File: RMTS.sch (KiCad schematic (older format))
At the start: 59 parts, among them J1 USB_B_Mini, J10 CONN_02, J2 Programmer, J3 Screw_Terminal_01x03, J4 Screw_Terminal_01x04, J5 Screw_Terminal_01x02, J6 Screw_Terminal_01x02, J7 Micro_SD_Card_Det_Hirose_DM3AT, J9 CONN_02, Q1 PMV20ENR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

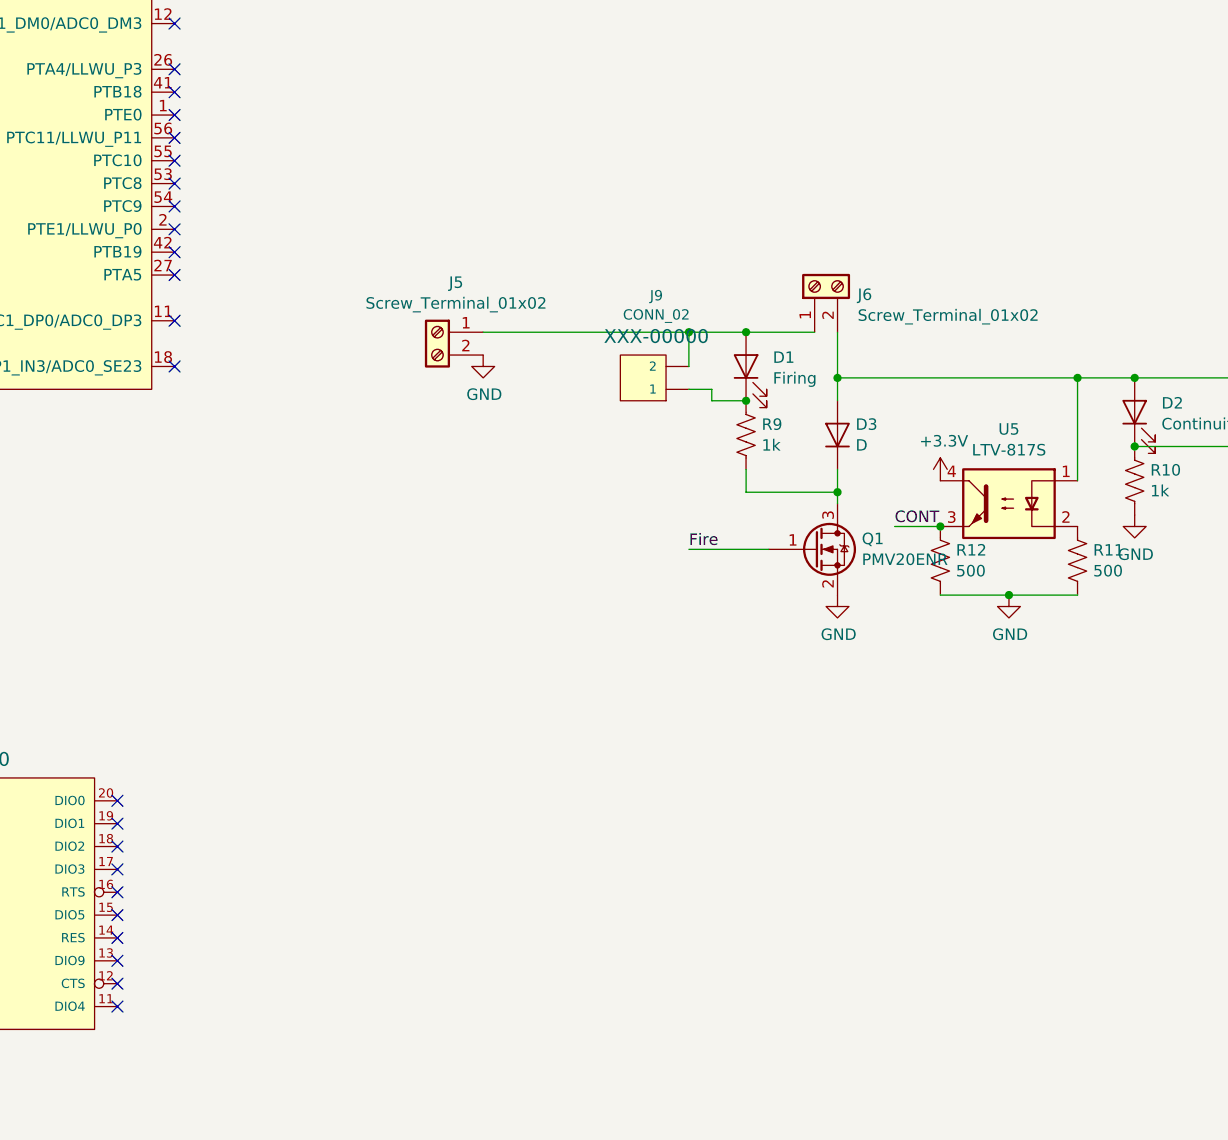
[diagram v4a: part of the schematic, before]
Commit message: Flipped SD card, added external firing circuit
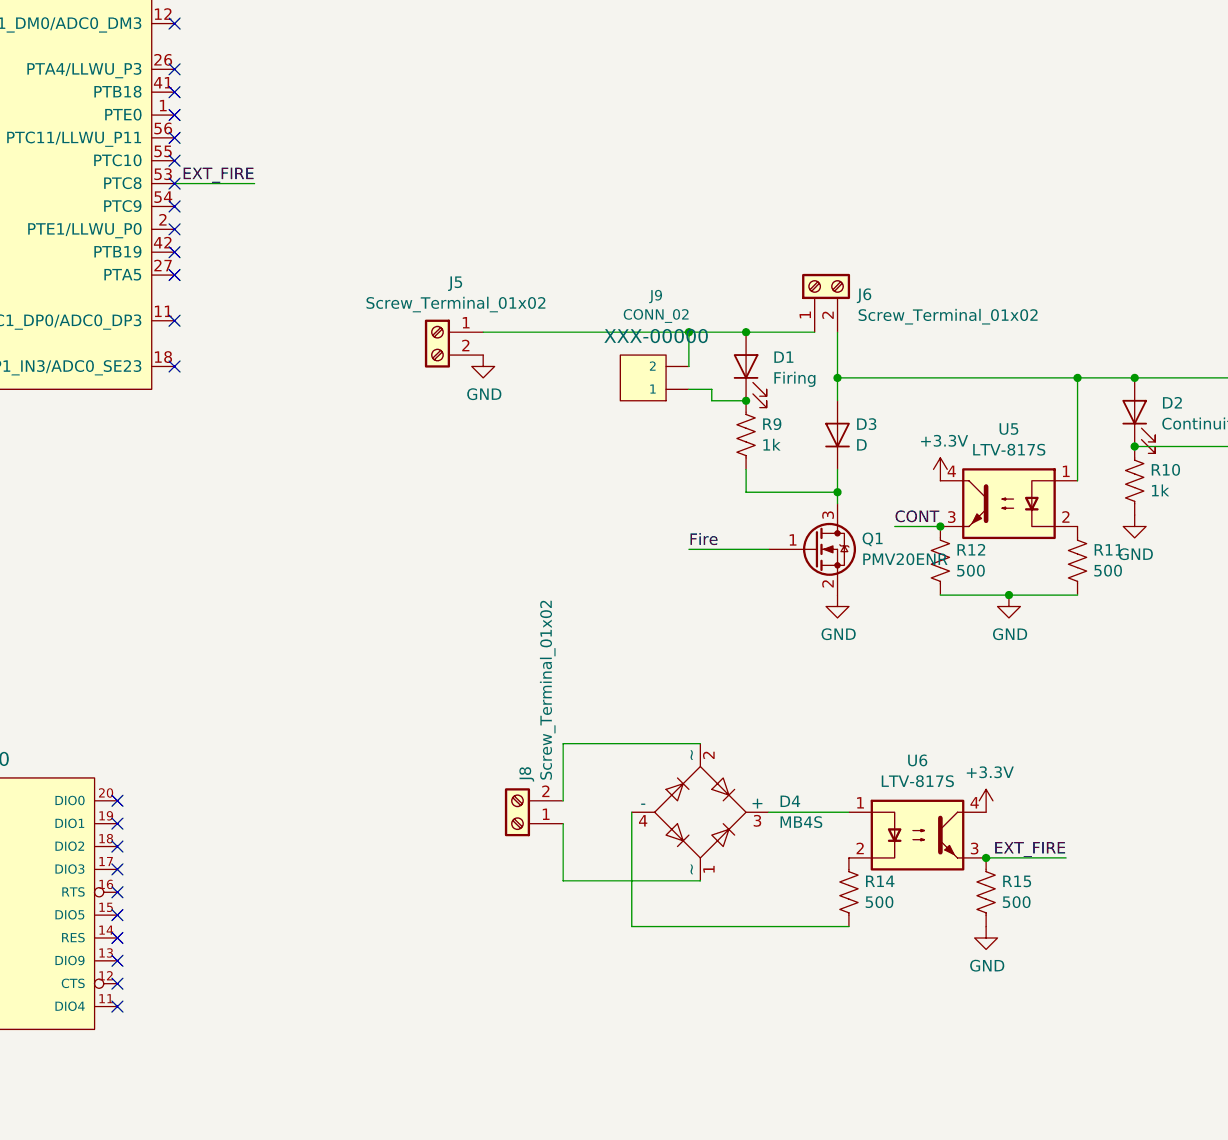
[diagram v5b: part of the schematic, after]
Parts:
- added D4: MB4S, Package_TO_SOT_SMD:TO-269AA, symbol Diode_Bridge:MB4S
- added J8: Screw_Terminal_01x02, Connectors:SCREWTERMINAL-3.5MM-2, symbol Connector:Screw_Terminal_01x02
- added R14, R15: 500, Resistor_SMD:R_0805_2012Metric_Pad1.15x1.40mm_HandSolder, symbol Device:R_US
- added U6: LTV-817S, Package_DIP:SMDIP-4_W9.53mm, symbol Isolator:LTV-817S
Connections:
- net +3V3: now also U6.4
- net GND: now also R15.2
- net EXT_FIRE: now reaches U2.53 (PTC8)
- net EXT_FIRE: now also R15.1, U6.3
- new net: D4.1 (~~), J8.1 (Pin_1)
- new net: D4.2 (~~), J8.2 (Pin_2)
- new net: D4.3 (+), U6.1
- new net: D4.4 (-), R14.2
- new net: R14.1, U6.2
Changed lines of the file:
@@
 	1    0    0    -1
 $EndComp
+$Comp
+L Diode_Bridge:MB4S D4
+U 1 1 5E5D5D8B
+P 12750 7550
+F 0 "D4" H 13094 7596 50  0000 L CNN
+F 1 "MB4S" H 13094 7505 50  0000 L CNN
+F 2 "Package_TO_SOT_SMD:TO-269AA" H 12900 7675 50  0001 L CNN
+F 3 "http://www.vishay.com/docs/88661/mb2s.pdf" H 12750 7550 50  0001 C CNN
+	1    12750 7550
+	1    0    0    -1
+$EndComp
+$Comp
+L Isolator:LTV-817S U6
+U 1 1 5E5D8E8B
+P 13700 7650
+F 0 "U6" H 13700 7975 50  0000 C CNN
+F 1 "LTV-817S" H 13700 7884 50  0000 C CNN
+F 2 "Package_DIP:SMDIP-4_W9.53mm" H 13700 7350 50  0001 C CNN
+F 3 "http://www.us.liteon.com/downloads/LTV-817-827-847.PDF" H 13350 7950 50  0001 C CNN
+	1    13700 7650
+	1    0    0    -1
+$EndComp
+$Comp
+L Device:R_US R14
+U 1 1 5E5DAC83
+P 13400 7900
+F 0 "R14" H 13468 7946 50  0000 L CNN
+F 1 "500" H 13468 7855 50  0000 L CNN
+F 2 "Resistor_SMD:R_0805_2012Metric_Pad1.15x1.40mm_HandSolder" V 13440 7890 50  0001 C CNN
+F 3 "~" H 13400 7900 50  0001 C CNN
+	1    13400 7900
+	1    0    0    -1
+$EndComp
+Wire Wire Line
+	12450 7550 12450 8050
+Wire Wire Line
+	12150 7250 12750 7250
+Wire Wire Line
+	12150 7600 12150 7850
+Wire Wire Line
+	12150 7850 12750 7850
+$Comp
+L power:+3.3V #PWR0146
+U 1 1 5E6123B3
+P 14000 7550
+F 0 "#PWR0146" H 14000 7400 50  0001 C CNN
+F 1 "+3.3V" H 14015 7723 50  0000 C CNN
+F 2 "" H 14000 7550 50  0001 C CNN
+F 3 "" H 14000 7550 50  0001 C CNN
+	1    14000 7550
+	1    0    0    -1
+$EndComp
+$Comp
+L Device:R_US R15
+U 1 1 5E612D46
+P 14000 7900
+F 0 "R15" H 14068 7946 50  0000 L CNN
+F 1 "500" H 14068 7855 50  0000 L CNN
+F 2 "Resistor_SMD:R_0805_2012Metric_Pad1.15x1.40mm_HandSolder" V 14040 7890 50  0001 C CNN
+F 3 "~" H 14000 7900 50  0001 C CNN
+	1    14000 7900
+	1    0    0    -1
+$EndComp
+$Comp
+L power:GND #PWR0147
+U 1 1 5E6138A0
+P 14000 8050
+F 0 "#PWR0147" H 14000 7800 50  0001 C CNN
+F 1 "GND" H 14005 7877 50  0000 C CNN
+F 2 "" H 14000 8050 50  0001 C CNN
+F 3 "" H 14000 8050 50  0001 C CNN
+	1    14000 8050
+	1    0    0    -1
+$EndComp
+Wire Wire Line
+	12450 8050 13400 8050
+Wire Wire Line
+	13050 7550 13400 7550
+Text Label 14350 7750 2    50   ~ 0
+EXT_FIRE
+Connection ~ 14000 7750
+Wire Wire Line
+	14000 7750 14350 7750
+Text Label 10800 4800 2    50   ~ 0
+EXT_FIRE
+Wire Wire Line
+	12150 7500 12150 7250
+$Comp
+L Connector:Screw_Terminal_01x02 J8
+U 1 1 5E5D4799
+P 11950 7600
+F 0 "J8" V 11914 7412 50  0000 R CNN
+F 1 "Screw_Terminal_01x02" V 11823 7412 50  0000 R CNN
+F 2 "Connectors:SCREWTERMINAL-3.5MM-2" H 11950 7600 50  0001 C CNN
+F 3 "~" H 11950 7600 50  0001 C CNN
+	1    11950 7600
+	-1   0    0    1
+$EndComp
+Wire Wire Line
+	10450 4800 10800 4800
 $EndSCHEMATC

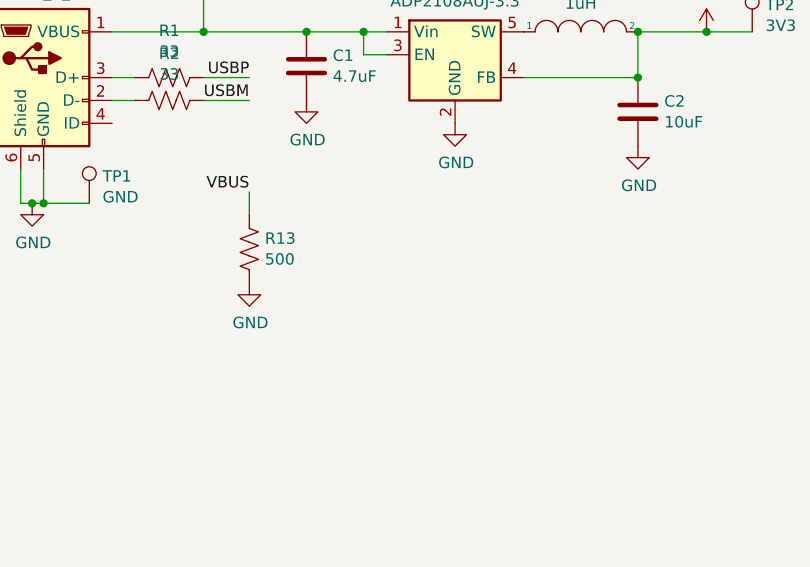
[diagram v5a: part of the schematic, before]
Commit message: Added power LED, moved labels, cleaned up some traces
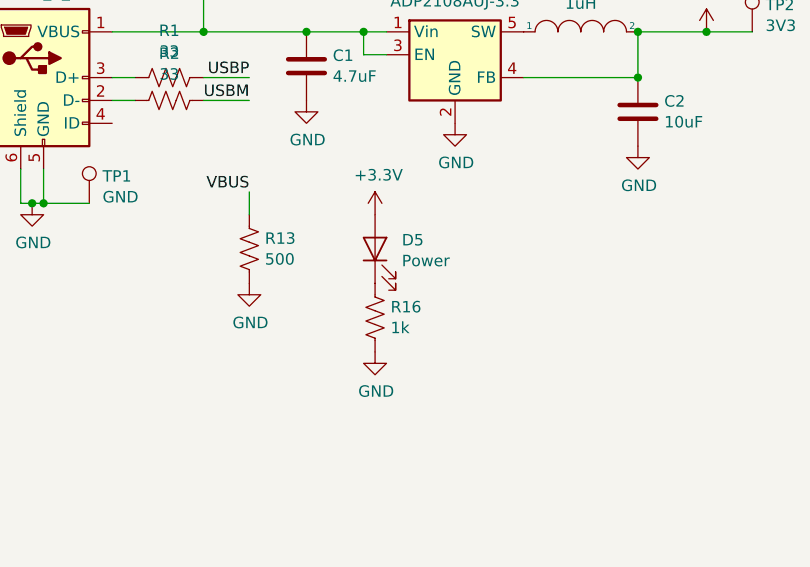
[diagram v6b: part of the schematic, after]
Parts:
- added D5: Power, LED_SMD:LED_0805_2012Metric_Pad1.15x1.40mm_HandSolder, symbol Device:LED
- added R16: 1k, Resistor_SMD:R_0805_2012Metric_Pad1.15x1.40mm_HandSolder, symbol Device:R_US
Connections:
- net +3V3: now also D5.2 (A)
- net GND: now also R16.2
- new net: D5.1 (K), R16.1
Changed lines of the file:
@@
 Wire Wire Line
 	10450 4800 10800 4800
+$Comp
+L Device:LED D5
+U 1 1 5E633442
+P 2450 2200
+F 0 "D5" V 2489 2083 50  0000 R CNN
+F 1 "Power" V 2398 2083 50  0000 R CNN
+F 2 "LED_SMD:LED_0805_2012Metric_Pad1.15x1.40mm_HandSolder" H 2450 2200 50  0001 C CNN
+F 3 "~" H 2450 2200 50  0001 C CNN
+	1    2450 2200
+	0    -1   -1   0
+$EndComp
+$Comp
+L Device:R_US R16
+U 1 1 5E6337F5
+P 2450 2500
+F 0 "R16" H 2518 2546 50  0000 L CNN
+F 1 "1k" H 2518 2455 50  0000 L CNN
+F 2 "Resistor_SMD:R_0805_2012Metric_Pad1.15x1.40mm_HandSolder" V 2490 2490 50  0001 C CNN
+F 3 "~" H 2450 2500 50  0001 C CNN
+	1    2450 2500
+	1    0    0    -1
+$EndComp
+$Comp
+L power:GND #PWR0148
+U 1 1 5E63654D
+P 2450 2650
+F 0 "#PWR0148" H 2450 2400 50  0001 C CNN
+F 1 "GND" H 2455 2477 50  0000 C CNN
+F 2 "" H 2450 2650 50  0001 C CNN
+F 3 "" H 2450 2650 50  0001 C CNN
+	1    2450 2650
+	1    0    0    -1
+$EndComp
+$Comp
+L power:+3.3V #PWR0149
+U 1 1 5E64594C
+P 2450 2050
+F 0 "#PWR0149" H 2450 1900 50  0001 C CNN
+F 1 "+3.3V" H 2465 2223 50  0000 C CNN
+F 2 "" H 2450 2050 50  0001 C CNN
+F 3 "" H 2450 2050 50  0001 C CNN
+	1    2450 2050
+	1    0    0    -1
+$EndComp
 $EndSCHEMATC

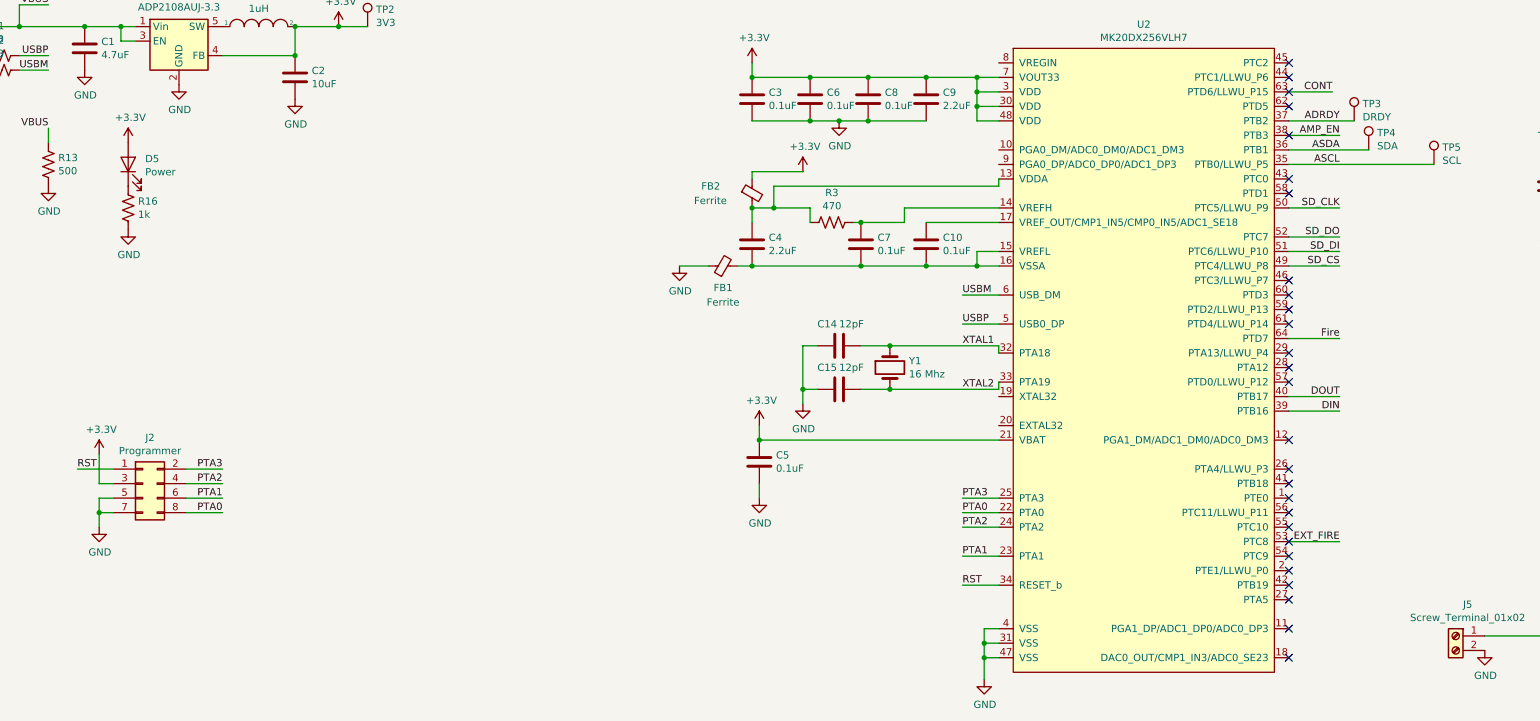
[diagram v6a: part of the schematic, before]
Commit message: Added status LED, hid labels
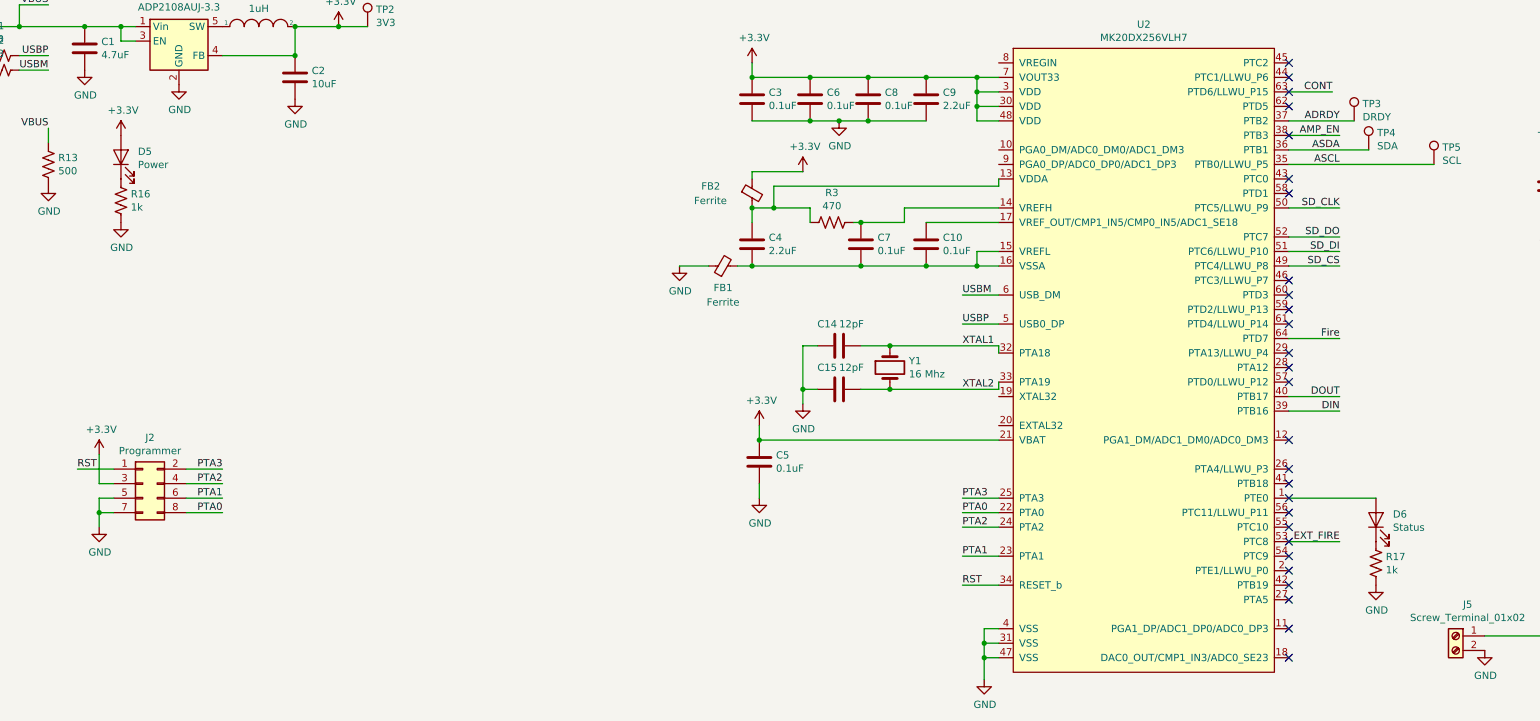
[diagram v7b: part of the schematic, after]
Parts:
- added D6: Status, LED_SMD:LED_0805_2012Metric_Pad1.15x1.40mm_HandSolder, symbol Device:LED
- added R17: 1k, Resistor_SMD:R_0805_2012Metric_Pad1.15x1.40mm_HandSolder, symbol Device:R_US
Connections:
- net GND: now also R17.2
- net at U2.1 (PTE0): now also D6.2 (A)
- new net: D6.1 (K), R17.1
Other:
- moved on the sheet: D5, R16
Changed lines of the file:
@@
 L Device:LED D5
 U 1 1 5E633442
-P 2450 2200
-F 0 "D5" V 2489 2083 50  0000 R CNN
-F 1 "Power" V 2398 2083 50  0000 R CNN
-F 2 "LED_SMD:LED_0805_2012Metric_Pad1.15x1.40mm_HandSolder" H 2450 2200 50  0001 C CNN
-F 3 "~" H 2450 2200 50  0001 C CNN
-	1    2450 2200
+P 2400 2150
+F 0 "D5" V 2439 2033 50  0000 R CNN
+F 1 "Power" V 2348 2033 50  0000 R CNN
+F 2 "LED_SMD:LED_0805_2012Metric_Pad1.15x1.40mm_HandSolder" H 2400 2150 50  0001 C CNN
+F 3 "~" H 2400 2150 50  0001 C CNN
+	1    2400 2150
 	0    -1   -1   0
 $EndComp
@@
 L Device:R_US R16
 U 1 1 5E6337F5
-P 2450 2500
-F 0 "R16" H 2518 2546 50  0000 L CNN
-F 1 "1k" H 2518 2455 50  0000 L CNN
-F 2 "Resistor_SMD:R_0805_2012Metric_Pad1.15x1.40mm_HandSolder" V 2490 2490 50  0001 C CNN
-F 3 "~" H 2450 2500 50  0001 C CNN
-	1    2450 2500
+P 2400 2450
+F 0 "R16" H 2468 2496 50  0000 L CNN
+F 1 "1k" H 2468 2405 50  0000 L CNN
+F 2 "Resistor_SMD:R_0805_2012Metric_Pad1.15x1.40mm_HandSolder" V 2440 2440 50  0001 C CNN
+F 3 "~" H 2400 2450 50  0001 C CNN
+	1    2400 2450
 	1    0    0    -1
 $EndComp
@@
 L power:GND #PWR0148
 U 1 1 5E63654D
-P 2450 2650
-F 0 "#PWR0148" H 2450 2400 50  0001 C CNN
-F 1 "GND" H 2455 2477 50  0000 C CNN
-F 2 "" H 2450 2650 50  0001 C CNN
-F 3 "" H 2450 2650 50  0001 C CNN
-	1    2450 2650
+P 2400 2600
+F 0 "#PWR0148" H 2400 2350 50  0001 C CNN
+F 1 "GND" H 2405 2427 50  0000 C CNN
+F 2 "" H 2400 2600 50  0001 C CNN
+F 3 "" H 2400 2600 50  0001 C CNN
+	1    2400 2600
 	1    0    0    -1
 $EndComp
@@
 L power:+3.3V #PWR0149
 U 1 1 5E64594C
-P 2450 2050
-F 0 "#PWR0149" H 2450 1900 50  0001 C CNN
-F 1 "+3.3V" H 2465 2223 50  0000 C CNN
-F 2 "" H 2450 2050 50  0001 C CNN
-F 3 "" H 2450 2050 50  0001 C CNN
-	1    2450 2050
+P 2400 2000
+F 0 "#PWR0149" H 2400 1850 50  0001 C CNN
+F 1 "+3.3V" H 2415 2173 50  0000 C CNN
+F 2 "" H 2400 2000 50  0001 C CNN
+F 3 "" H 2400 2000 50  0001 C CNN
+	1    2400 2000
 	1    0    0    -1
 $EndComp
+$Comp
+L Device:LED D6
+U 1 1 5E6AA981
+P 11050 4650
+F 0 "D6" V 11089 4533 50  0000 R CNN
+F 1 "Status" V 10998 4533 50  0000 R CNN
+F 2 "LED_SMD:LED_0805_2012Metric_Pad1.15x1.40mm_HandSolder" H 11050 4650 50  0001 C CNN
+F 3 "~" H 11050 4650 50  0001 C CNN
+	1    11050 4650
+	0    -1   -1   0
+$EndComp
+$Comp
+L Device:R_US R17
+U 1 1 5E6AAE55
+P 11050 4950
+F 0 "R17" H 11118 4996 50  0000 L CNN
+F 1 "1k" H 11118 4905 50  0000 L CNN
+F 2 "Resistor_SMD:R_0805_2012Metric_Pad1.15x1.40mm_HandSolder" V 11090 4940 50  0001 C CNN
+F 3 "~" H 11050 4950 50  0001 C CNN
+	1    11050 4950
+	1    0    0    -1
+$EndComp
+$Comp
+L power:GND #PWR0150
+U 1 1 5E6AB42B
+P 11050 5100
+F 0 "#PWR0150" H 11050 4850 50  0001 C CNN
+F 1 "GND" H 11055 4927 50  0000 C CNN
+F 2 "" H 11050 5100 50  0001 C CNN
+F 3 "" H 11050 5100 50  0001 C CNN
+	1    11050 5100
+	1    0    0    -1
+$EndComp
+Wire Wire Line
+	10450 4500 11050 4500
 $EndSCHEMATC
